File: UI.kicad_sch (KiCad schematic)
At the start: 32 parts

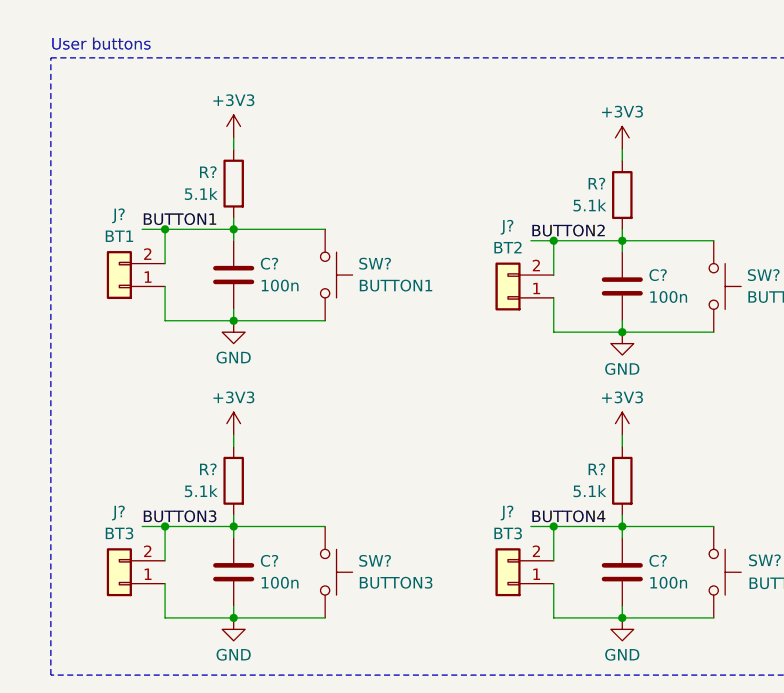
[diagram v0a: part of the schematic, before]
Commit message: Sistemato disaccoppiamento pulasnti, e aggiunto gyro i2c
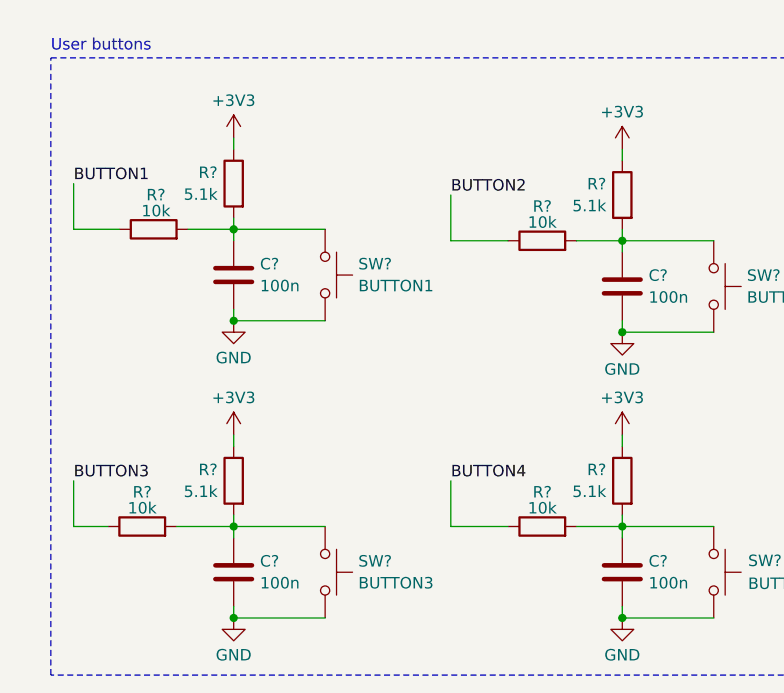
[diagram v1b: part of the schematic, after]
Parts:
- removed J?: BT2, Connector_JST:JST_XH_B2B-XH-A_1x02_P2.50mm_Vertical, symbol Connector_Generic:Conn_01x02
- removed J?: BT1, Connector_JST:JST_XH_B2B-XH-A_1x02_P2.50mm_Vertical, symbol Connector_Generic:Conn_01x02
- removed J? (x2): BT3, Connector_JST:JST_XH_B2B-XH-A_1x02_P2.50mm_Vertical, symbol Connector_Generic:Conn_01x02
- added R? (x4): 10k, Resistor_SMD:R_0805_2012Metric_Pad1.20x1.40mm_HandSolder, symbol Device:R
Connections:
- net BUTTON1: now also R?.1; no longer C?.1, R?.2, SW?.1
- net BUTTON2: now also R?.1; no longer C?.1, R?.2, SW?.1
- net BUTTON3: now also R?.1; no longer C?.1, R?.2, SW?.1
- net BUTTON4: now also R?.1; no longer C?.1, R?.2, SW?.1
- new net: C?.1, R?.2, R?.2, SW?.1 (x4)

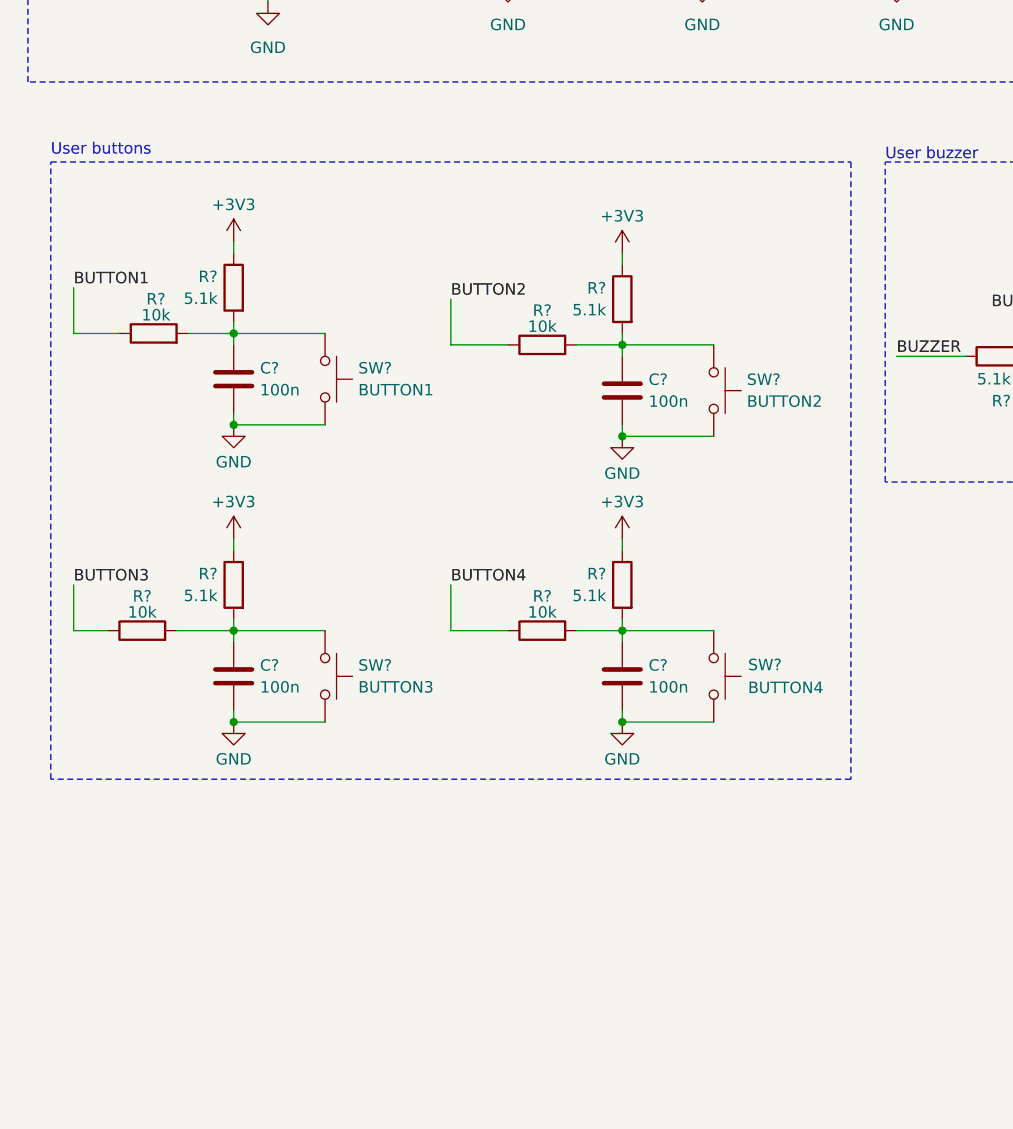
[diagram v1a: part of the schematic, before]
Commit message: Added MCU sheet + added a button on the UI sheet
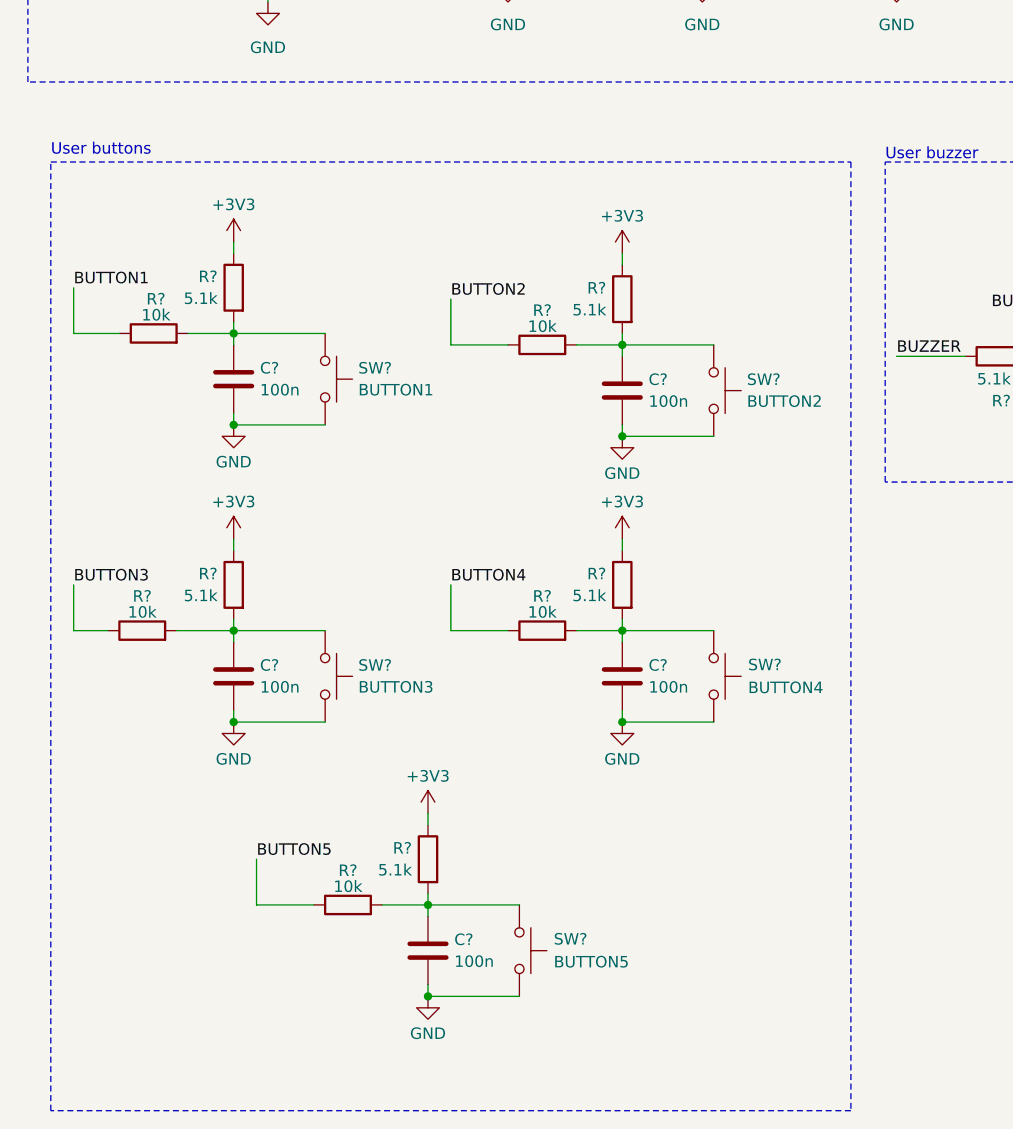
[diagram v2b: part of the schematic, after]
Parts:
- added C?: 100n, Capacitor_SMD:C_0805_2012Metric_Pad1.18x1.45mm_HandSolder, symbol Device:C
- added R?: 5.1k, Resistor_SMD:R_0805_2012Metric_Pad1.20x1.40mm_HandSolder, symbol Device:R
- added R?: 10k, Resistor_SMD:R_0805_2012Metric_Pad1.20x1.40mm_HandSolder, symbol Device:R
- added SW?: BUTTON5, Button_Switch_SMD:SW_SPST_SKQG_WithoutStem, symbol Switch:SW_Push
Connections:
- net +3V3: now also R?.1
- net GND: now also C?.2, SW?.2
- new net: C?.1, R?.2, R?.2, SW?.1
- new net BUTTON5: R?.1

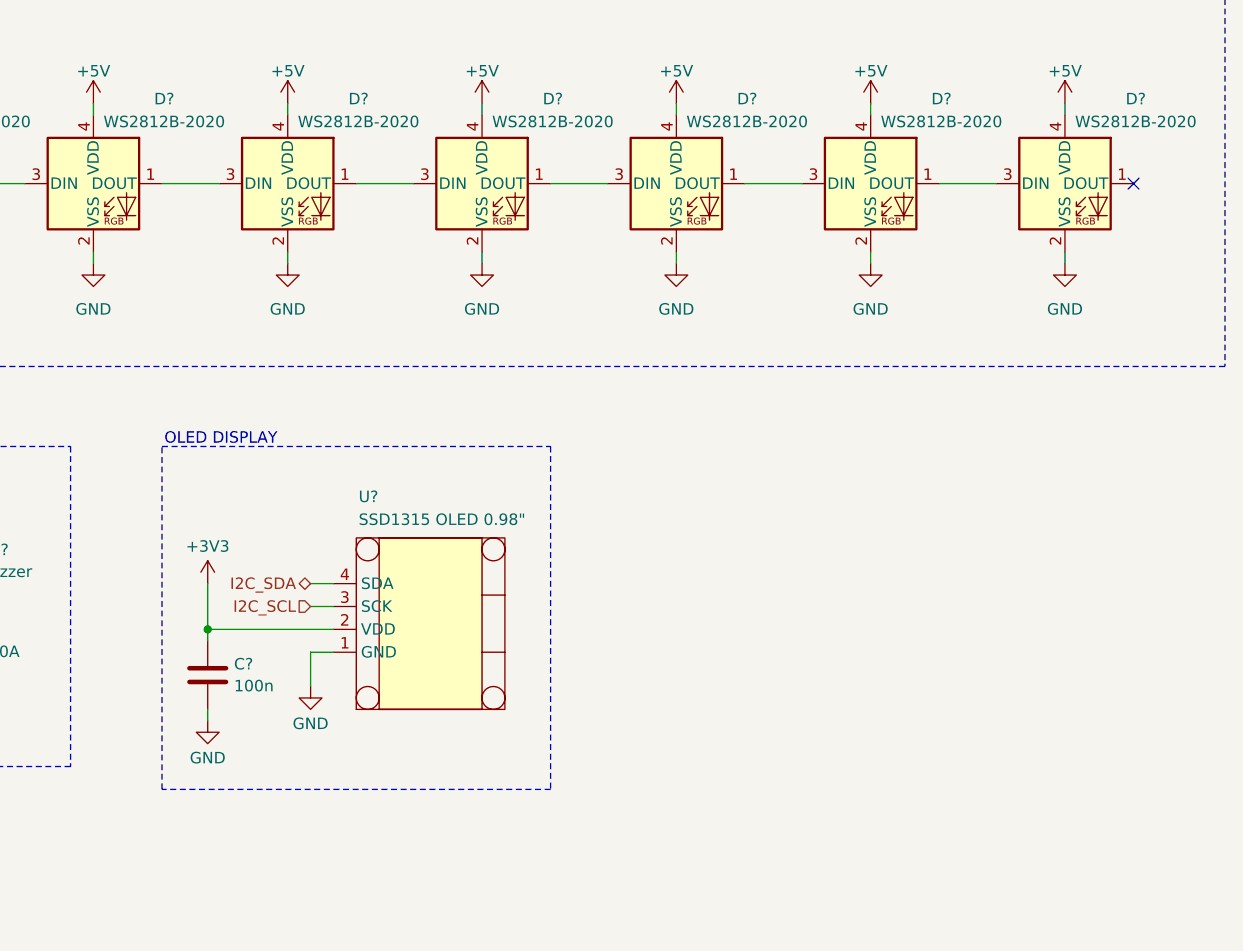
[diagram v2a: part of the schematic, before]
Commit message: Connected the nucleo to local nets
 - I created all the local lables to the MCU schematic and connected them to the corresponding pins of the Nucleo board.
 - I renumed the hierarchical sheets to be in order of importance
 - I added solder jumpers for making the board more versatile in some cases
 - Corrected the Nucleo pinout on the schematic symbol
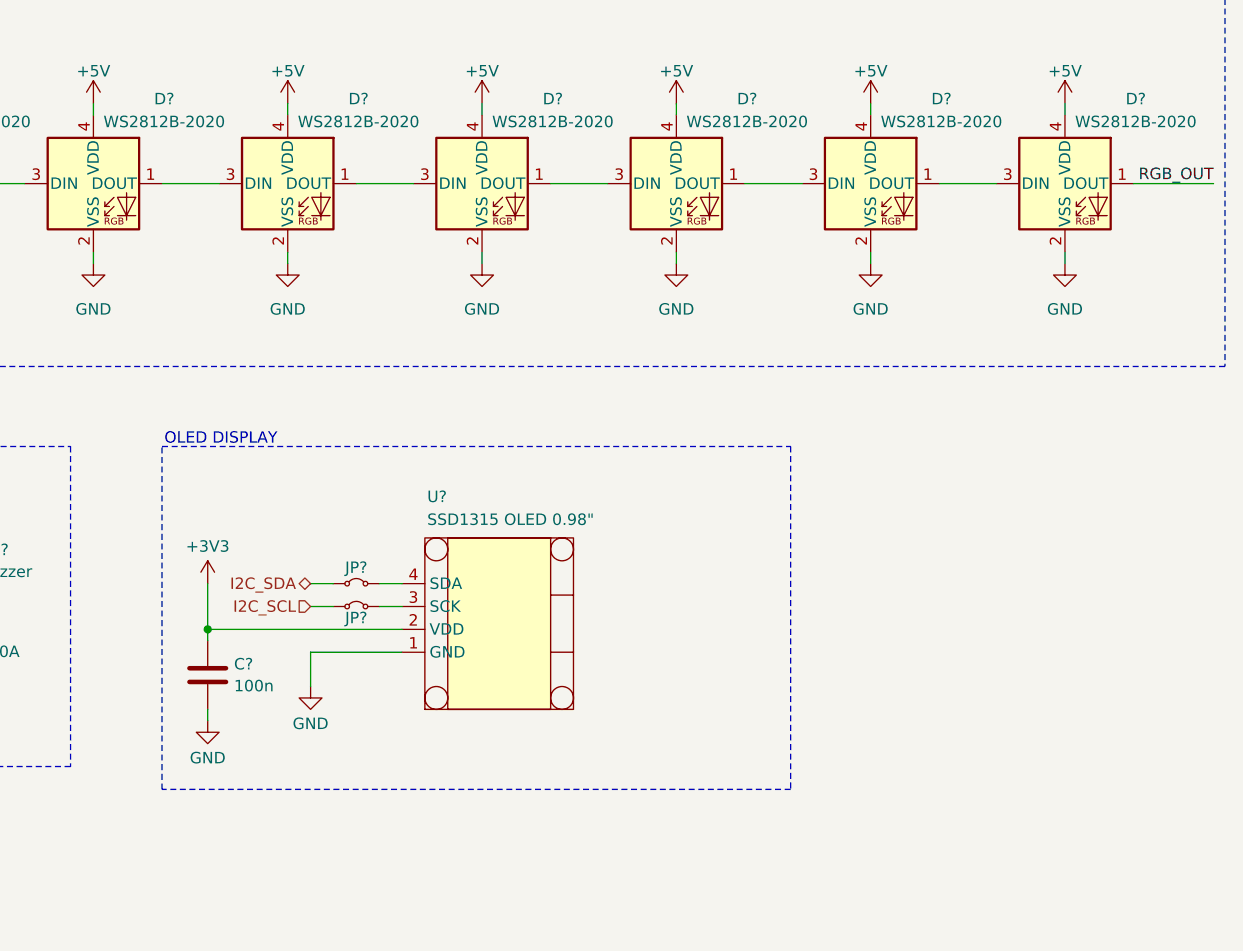
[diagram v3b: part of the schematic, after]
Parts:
- added JP? (x2): 0R, symbol Jumper:Jumper_2_Small_Bridged
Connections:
- net I2C_SCL: now also JP?.1 (A); no longer U?.3 (SCK)
- net I2C_SDA: now also JP?.1 (A); no longer U?.4 (SDA)
- net RGB_OUT: now reaches D?.1 (DOUT)
- new net: JP?.2 (B), U?.3 (SCK)
- new net: JP?.2 (B), U?.4 (SDA)
- no-connect marks 1 -> 0
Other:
- moved on the sheet: U?
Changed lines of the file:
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@@
 	(rectangle
 		(start 162.56 67.31)
-		(end 205.74 105.41)
+		(end 232.41 105.41)
 		(stroke
 			(width 0)
@@
 		(color 0 0 0 0)
 	)
-	(no_connect
-		(at 270.51 38.1)
-	)
 	(wire
 		(pts
@@
 	(wire
 		(pts
+			(xy 186.69 85.09) (xy 189.23 85.09)
+		)
+		(stroke
+			(width 0)
+			(type default)
+		)
+	)
+	(wire
+		(pts
 			(xy 38.1 109.22) (xy 38.1 110.49)
 		)
@@
 	(wire
 		(pts
+			(xy 270.51 38.1) (xy 279.4 38.1)
+		)
+		(stroke
+			(width 0)
+			(type default)
+		)
+	)
+	(wire
+		(pts
 			(xy 81.28 119.38) (xy 91.44 119.38)
 		)
@@
 	(wire
 		(pts
-			(xy 181.61 90.17) (xy 179.07 90.17)
+			(xy 189.23 90.17) (xy 179.07 90.17)
 		)
 		(stroke
@@
 	(wire
 		(pts
-			(xy 167.64 87.63) (xy 181.61 87.63)
+			(xy 167.64 87.63) (xy 189.23 87.63)
 		)
 		(stroke
@@
 	(wire
 		(pts
+			(xy 186.69 82.55) (xy 189.23 82.55)
+		)
+		(stroke
+			(width 0)
+			(type default)
+		)
+	)
+	(wire
+		(pts
 			(xy 59.69 139.7) (xy 59.69 140.97)
 		)
@@
 		)
 	)
+	(label "RGB_OUT"
+		(at 279.4 38.1 180)
+		(effects
+			(font
+				(size 1.27 1.27)
+			)
+			(justify right bottom)
+		)
+	)
 	(label "BUTTON1"
 		(at 20.32 81.28 0)
@@
 	(symbol
 		(lib_id "_MIA:oled_0.96{dblquote}_128x64px")
-		(at 191.77 87.63 90)
+		(at 199.39 87.63 90)
 		(unit 1)
 		(exclude_from_sim no)
@@
 		(dnp no)
 		(property "Reference" "U?"
-			(at 184.404 72.898 90)
+			(at 192.024 72.898 90)
 			(effects
 				(font
@@
 		)
 		(property "Value" "SSD1315 OLED 0.98\""
-			(at 184.404 75.438 90)
+			(at 192.024 75.438 90)
 			(effects
 				(font
@@
 		)
 		(property "Footprint" ""
-			(at 176.53 95.25 0)
+			(at 184.15 95.25 0)
 			(effects
 				(font
@@
 		)
 		(property "Datasheet" ""
-			(at 176.53 95.25 0)
+			(at 184.15 95.25 0)
 			(effects
 				(font
@@
 		)
 		(property "Description" ""
-			(at 191.77 87.63 0)
+			(at 199.39 87.63 0)
 			(effects
 				(font
@@
 		(dnp no)
 		(fields_autoplaced yes)
-		(property "Reference" "#PWR01"
+		(property "Reference" "#PWR?"
 			(at 59.69 143.51 0)
 			(effects
@@
 			(project "Educational-Board_MainBoard"
 				(path "/835b4df9-7d62-45f4-81d2-5a64fbc86f3c/4cd73753-9d62-4e71-9011-aaea0e9d47c0"
-					(reference "#PWR01")
+					(reference "#PWR?")
 					(unit 1)
 				)
@@
 	)
 	(symbol
+		(lib_id "Jumper:Jumper_2_Small_Bridged")
+		(at 184.15 85.09 0)
+		(unit 1)
+		(exclude_from_sim no)
+		(in_bom yes)
+		(on_board yes)
+		(dnp no)
+		(property "Reference" "JP?"
+			(at 184.15 86.36 0)
+			(effects
+				(font
+					(size 1.27 1.27)
+				)
+			)
+		)
+		(property "Value" "0R"
+			(at 184.15 82.55 0)
+			(effects
+				(font
+					(size 1.27 1.27)
+				)
+				(hide yes)
+			)
+		)
+		(property "Footprint" ""
+			(at 184.15 85.09 0)
+			(effects
+				(font
+					(size 1.27 1.27)
+				)
+				(hide yes)
+			)
+		)
+		(property "Datasheet" "~"
+			(at 184.15 85.09 0)
+			(effects
+				(font
+					(size 1.27 1.27)
+				)
+				(hide yes)
+			)
+		)
+		(property "Description" ""
+			(at 184.15 85.09 0)
+			(effects
+				(font
+					(size 1.27 1.27)
+				)
+			)
+		)
+		(pin "1"
+		)
+		(pin "2"
+		)
+		(instances
+			(project "Educational-Board_MainBoard"
+				(path "/835b4df9-7d62-45f4-81d2-5a64fbc86f3c/4cd73753-9d62-4e71-9011-aaea0e9d47c0"
+					(reference "JP?")
+					(unit 1)
+				)
+			)
+		)
+	)
+	(symbol
 		(lib_id "power:+5V")
 		(at 41.91 26.67 0)
@@
 	)
 	(symbol
+		(lib_id "Jumper:Jumper_2_Small_Bridged")
+		(at 184.15 82.55 0)
+		(unit 1)
+		(exclude_from_sim no)
+		(in_bom yes)
+		(on_board yes)
+		(dnp no)
+		(property "Reference" "JP?"
+			(at 184.15 80.772 0)
+			(effects
+				(font
+					(size 1.27 1.27)
+				)
+			)
+		)
+		(property "Value" "0R"
+			(at 184.15 80.01 0)
+			(effects
+				(font
+					(size 1.27 1.27)
+				)
+				(hide yes)
+			)
+		)
+		(property "Footprint" ""
+			(at 184.15 82.55 0)
+			(effects
+				(font
+					(size 1.27 1.27)
+				)
+				(hide yes)
+			)
+		)
+		(property "Datasheet" "~"
+			(at 184.15 82.55 0)
+			(effects
+				(font
+					(size 1.27 1.27)
+				)
+				(hide yes)
+			)
+		)
+		(property "Description" "Jumper, 2-pole, small symbol, bridged"
+			(at 184.15 82.55 0)
+			(effects
+				(font
+					(size 1.27 1.27)
+				)
+				(hide yes)
+			)
+		)
+		(pin "1"
+		)
+		(pin "2"
+		)
+		(instances
+			(project "Educational-Board_MainBoard"
+				(path "/835b4df9-7d62-45f4-81d2-5a64fbc86f3c/4cd73753-9d62-4e71-9011-aaea0e9d47c0"
+					(reference "JP?")
+					(unit 1)
+				)
+			)
+		)
+	)
+	(symbol
 		(lib_id "Transistor_FET:AO3400A")
 		(at 133.35 88.9 0)
@@
 		(dnp no)
 		(fields_autoplaced yes)
-		(property "Reference" "#PWR02"
+		(property "Reference" "#PWR?"
 			(at 59.69 166.37 0)
 			(effects
@@
 			(project "Educational-Board_MainBoard"
 				(path "/835b4df9-7d62-45f4-81d2-5a64fbc86f3c/4cd73753-9d62-4e71-9011-aaea0e9d47c0"
-					(reference "#PWR02")
+					(reference "#PWR?")
 					(unit 1)
 				)
